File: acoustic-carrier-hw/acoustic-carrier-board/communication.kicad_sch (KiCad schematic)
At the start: 0 parts

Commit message: [acoustic-carrier-board] Added ethernet PHY
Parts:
- added J3: 8P8C_Shielded, Connector_RJ:RJ45_RCH_RC01937, symbol Connector:8P8C_Shielded
- added U1: KSZ9031RNXCA, Package_DFN_QFN:QFN-48-1EP_7x7mm_P0.5mm_EP5.15x5.15mm, symbol Interface_Ethernet:KSZ9031RNXCA
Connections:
- new net GNDA: J3.SH

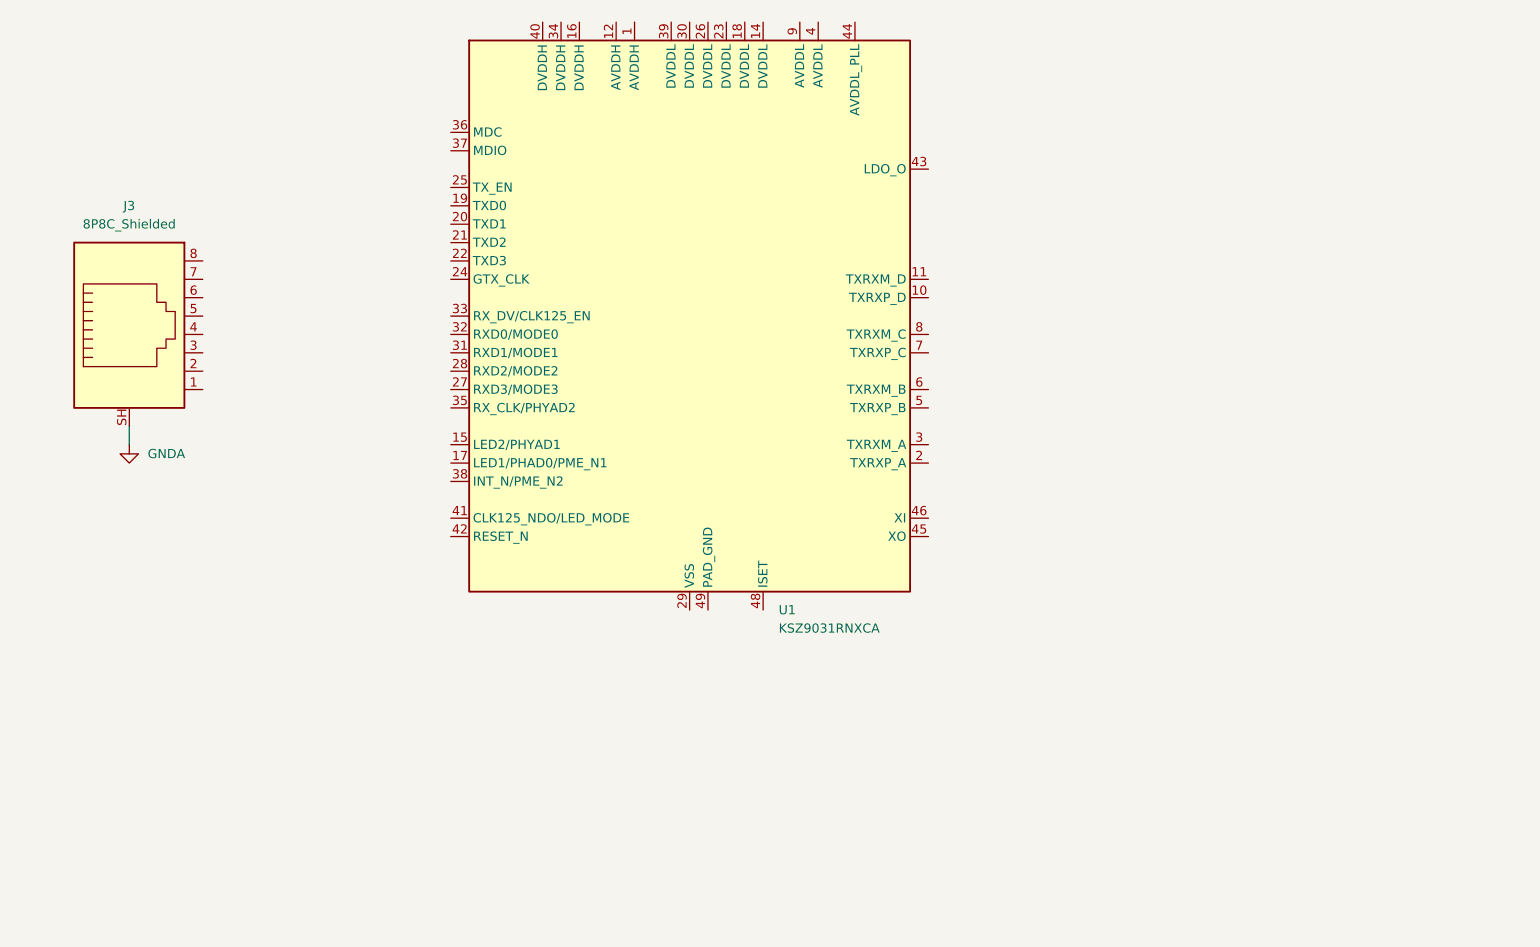
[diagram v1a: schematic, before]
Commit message: [carrier] Added decoupling to ethernet PHY
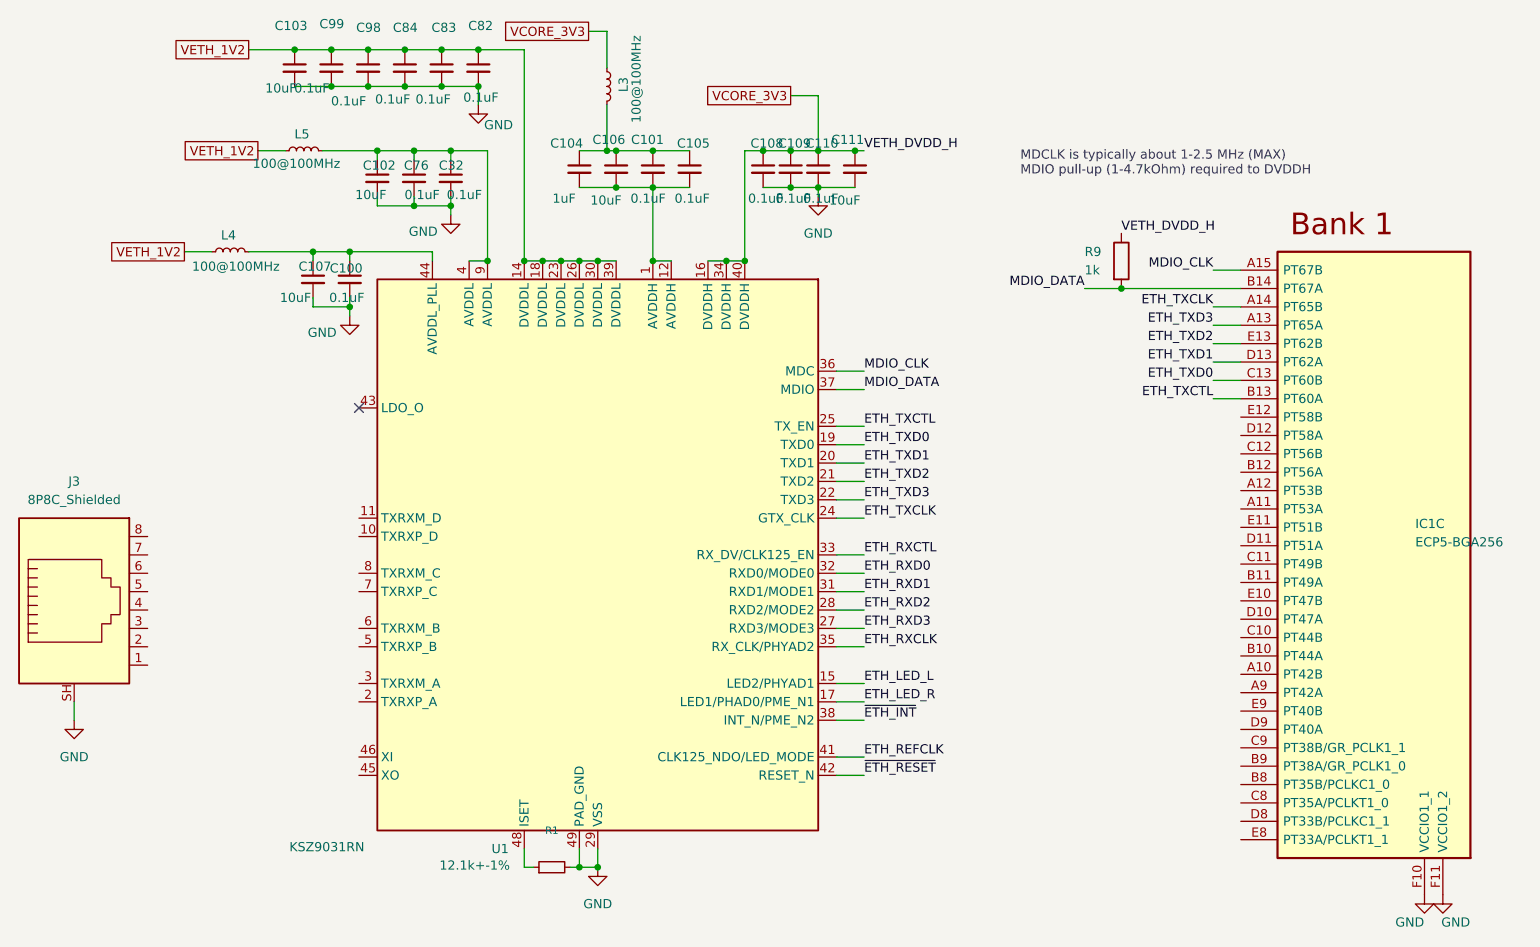
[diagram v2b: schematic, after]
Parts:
- added C100, C101, C105, C108, C109, C110, C32, C76, C82, C83, C84, C98, C99: 0.1uF, Capacitor_SMD:C_0402_1005Metric, symbol Device:C_Small
- added C102, C103, C106, C107, C111: 10uF, Capacitor_SMD:C_0603_1608Metric, symbol Device:C_Small
- added C104: 1uF, Capacitor_SMD:C_0805_2012Metric, symbol Device:C_Small
- added IC1: ECP5-BGA256, BGA256C80P16X16_1400X1400X170, symbol ecp5bga256:ECP5-BGA256
- added L3, L4, L5: 100@100MHz, Inductor_SMD:L_0805_2012Metric, symbol Device:L_Small
- added R1: 12.1k+-1%, Resistor_SMD:R_0603_1608Metric, symbol Device:R_Small
- added R9: 1k, Resistor_SMD:R_0805_2012Metric_Pad1.20x1.40mm_HandSolder, symbol Device:R
- U1: value KSZ9031RNXCA -> KSZ9031RN; LPN (none) -> C461575; MPN (none) -> KSZ9031RNXCC
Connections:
- net GNDA is gone; now on net GND: J3.SH
- net at U1.1 (AVDDH): now also U1.12 (AVDDH), C101.2, C104.2, C105.2, C106.2
- net VETH_1V2: now reaches U1.14 (DVDDL)
- net VETH_1V2: now also U1.18 (DVDDL), U1.23 (DVDDL), U1.26 (DVDDL), U1.30 (DVDDL), U1.39 (DVDDL), C103.1, C82.1, C83.1, C84.1, C98.1, C99.1, L4.2, L5.2
- net ETH_LED_L: now reaches U1.15 (LED2/PHYAD1)
- net VCORE_3V3: now reaches U1.16 (DVDDH)
- net VCORE_3V3: now also U1.34 (DVDDH), U1.40 (DVDDH), C108.1, C109.1, C110.1, C111.1, L3.2, R9.1
- net ETH_LED_R: now reaches U1.17 (LED1/PHAD0/PME_N1)
- net ETH_TXD0: now reaches U1.19 (TXD0)
- net ETH_TXD0: now also IC1.C13 (PT60B)
- net ETH_TXD1: now reaches U1.20 (TXD1)
- net ETH_TXD1: now also IC1.D13 (PT62A)
- net ETH_TXD2: now reaches U1.21 (TXD2)
- net ETH_TXD2: now also IC1.E13 (PT62B)
- net ETH_TXD3: now reaches U1.22 (TXD3)
- net ETH_TXD3: now also IC1.A13 (PT65A)
- net ETH_TXCLK: now reaches U1.24 (GTX_CLK)
- net ETH_TXCLK: now also IC1.A14 (PT65B)
- net ETH_TXCTL: now reaches U1.25 (TX_EN)
- net ETH_TXCTL: now also IC1.B13 (PT60A)
- net ETH_RXD3: now reaches U1.27 (RXD3/MODE3)
- net ETH_RXD2: now reaches U1.28 (RXD2/MODE2)
- net GND: now reaches U1.29 (VSS)
- net GND: now also U1.49 (PAD_GND), C100.2, C102.2, C103.2, C107.2, C108.2, C109.2, C110.2, C111.2, C32.2, C76.2, C82.2, C83.2, C84.2, C98.2, C99.2, IC1.F10 (VCCIO1_1), IC1.F11 (VCCIO1_2), R1.2
- net ETH_RXD1: now reaches U1.31 (RXD1/MODE1)
- net ETH_RXD0: now reaches U1.32 (RXD0/MODE0)
- net ETH_RXCTL: now reaches U1.33 (RX_DV/CLK125_EN)
- net ETH_RXCLK: now reaches U1.35 (RX_CLK/PHYAD2)
- net MDIO_CLK: now reaches U1.36 (MDC)
- net MDIO_CLK: now also IC1.A15 (PT67B)
- net MDIO_DATA: now reaches U1.37 (MDIO)
- net MDIO_DATA: now also IC1.B14 (PT67A), R9.2
- net ~{ETH_INT}: now reaches U1.38 (INT_N/PME_N2)
- net at U1.4 (AVDDL): now also U1.9 (AVDDL), C102.1, C32.1, C76.1, L5.1
- net ETH_REFCLK: now reaches U1.41 (CLK125_NDO/LED_MODE)
- net ~{ETH_RESET}: now reaches U1.42 (RESET_N)
- net at U1.44 (AVDDL_PLL): now also C100.1, C107.1, L4.1
- net at U1.48 (ISET): now also R1.1
- new net: C101.1, C104.1, C105.1, C106.1, L3.1
- no-connect marks 0 -> 1
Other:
- note added: "MDCLK is typically about 1-2.5 MHz (MAX) MDIO pull-up (1-4.7kOhm) required to DVDDH"
- moved on the sheet: J3, U1

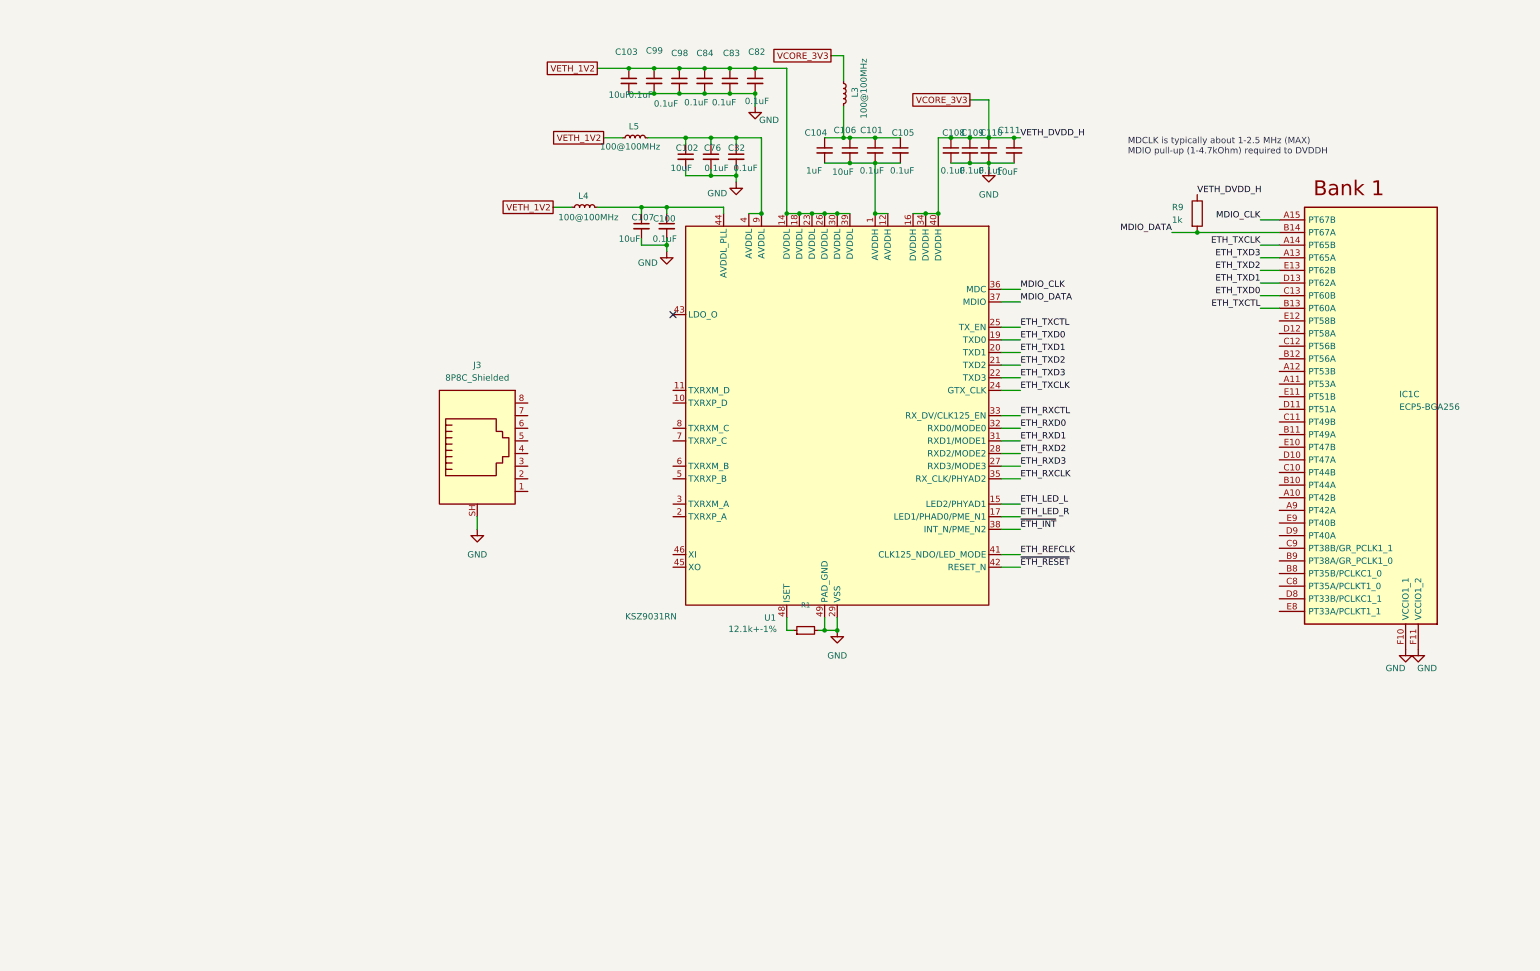
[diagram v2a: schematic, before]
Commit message: [carrier] Finished ethernet
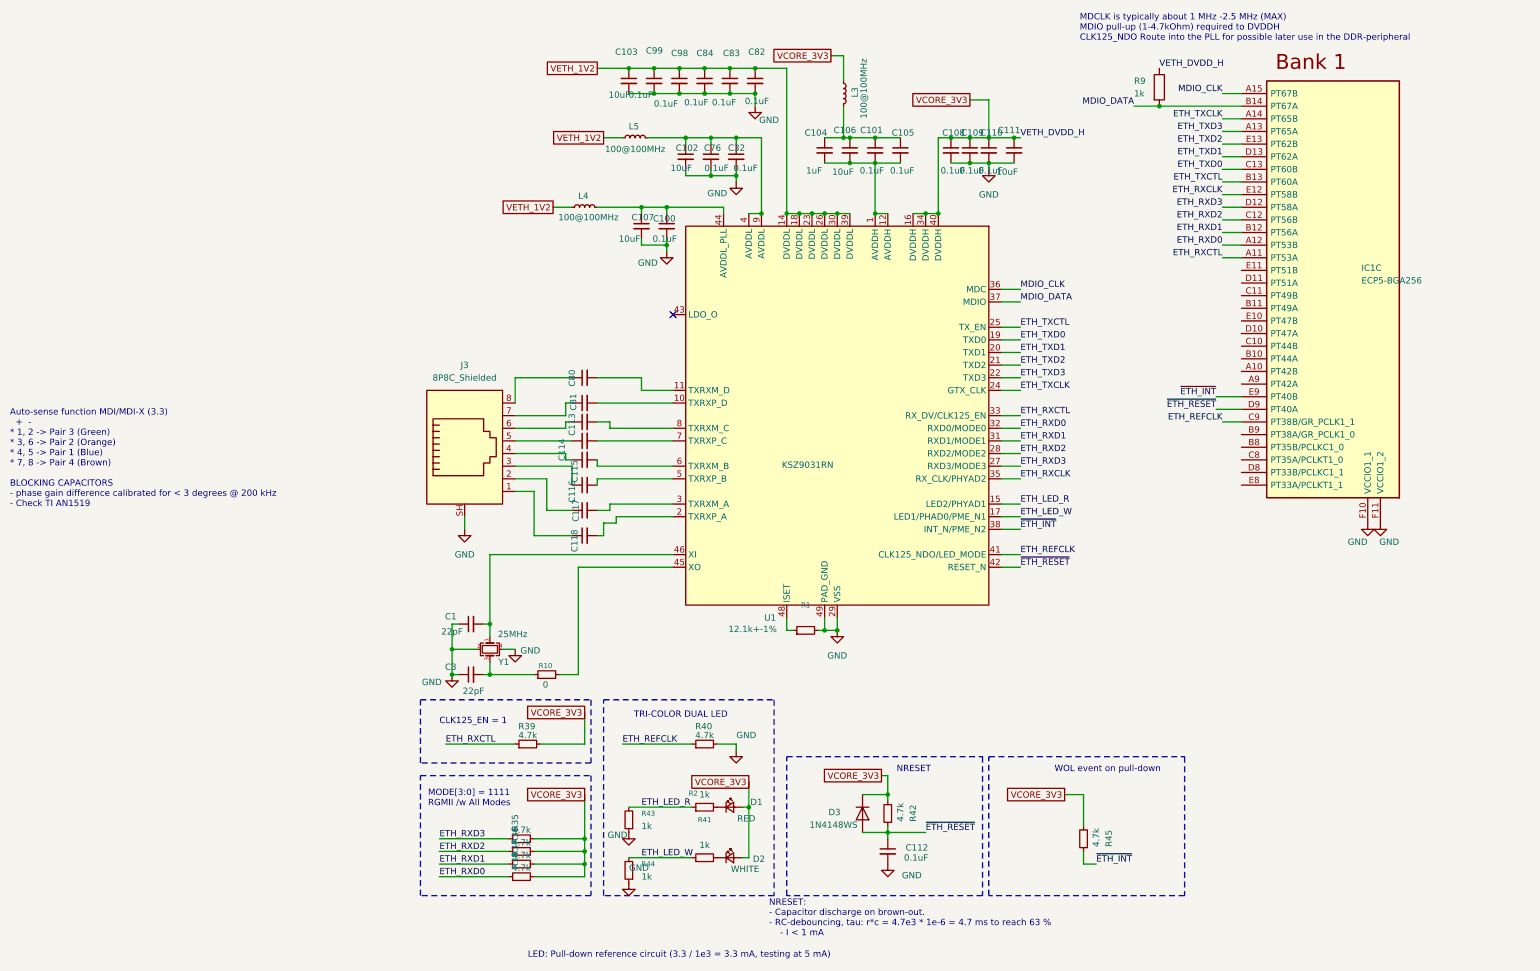
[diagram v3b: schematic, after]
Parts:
- added C1, C3: 22pF, Capacitor_SMD:C_0402_1005Metric, symbol Device:C_Small
- added C112: 0.1uF, Capacitor_SMD:C_0402_1005Metric, symbol Device:C_Small
- added C113, C114, C115, C116, C117, C118, C80, C81: 100 nF +-5%, Capacitor_SMD:C_0603_1608Metric_Pad1.08x0.95mm_HandSolder, symbol Device:C_Small
- added D1: RED, Diode_SMD:D_0603_1608Metric, symbol Device:LED_Small
- added D2: WHITE, Diode_SMD:D_0603_1608Metric, symbol Device:LED_Small
- added D3: 1N4148WS, Diode_SMD:D_SOD-323, symbol Diode:1N4148WS
- added R10: 0, Resistor_SMD:R_0402_1005Metric_Pad0.72x0.64mm_HandSolder, symbol Device:R_Small
- added R2, R41, R43, R44: 1k, Resistor_SMD:R_0402_1005Metric, symbol Device:R_Small
- added R35, R36, R37, R38, R39, R40, R42, R45: 4.7k, Resistor_SMD:R_0402_1005Metric, symbol Device:R_Small
- added Y1: 25MHz, Crystal:Crystal_SMD_3225-4Pin_3.2x2.5mm, symbol Device:Crystal_GND24_Small
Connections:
- net ETH_LED_L is gone; now on net ETH_LED_R: U1.15 (LED2/PHYAD1)
- net ETH_LED_R: now also R2.1, R43.2; no longer U1.17 (LED1/PHAD0/PME_N1)
- net ETH_REFCLK: now also IC1.C9 (PT38B/GR_PCLK1_1), R40.1
- net ETH_RXCLK: now also IC1.E12 (PT58B)
- net ETH_RXCTL: now also IC1.A11 (PT53A), R39.1
- net ETH_RXD0: now also IC1.A12 (PT53B), R38.1
- net ETH_RXD1: now also IC1.B12 (PT56A), R37.1
- net ETH_RXD2: now also IC1.C12 (PT56B), R36.1
- net ETH_RXD3: now also IC1.D12 (PT58A), R35.1
- net GND: now also C1.1, C112.2, C3.1, R40.2, R43.1, R44.1, Y1.2, Y1.4
- net VCORE_3V3: now also D1.2 (A), D2.2 (A), D3.1 (K), R35.2, R36.2, R37.2, R38.2, R39.2, R42.2, R45.2
- net ~{ETH_INT}: now also IC1.E9 (PT40B), R45.1
- net ~{ETH_RESET}: now also IC1.D9 (PT40A), C112.1, D3.2 (A), R42.1
- net at J3.1: now also C118.1
- net at J3.2: now also C117.1
- net at J3.3: now also C116.1
- net at J3.4: now also C115.1
- net at J3.5: now also C114.1
- net at J3.6: now also C113.1
- net at J3.7: now also C81.1
- net at J3.8: now also C80.1
- net at U1.10 (TXRXP_D): now also C81.2
- net at U1.11 (TXRXM_D): now also C80.2
- net at U1.2 (TXRXP_A): now also C118.2
- net at U1.3 (TXRXM_A): now also C117.2
- net at U1.45 (XO): now also R10.2
- net at U1.46 (XI): now also C1.2, Y1.1
- net at U1.5 (TXRXP_B): now also C116.2
- net at U1.6 (TXRXM_B): now also C115.2
- net at U1.7 (TXRXP_C): now also C114.2
- net at U1.8 (TXRXM_C): now also C113.2
- new net: C3.2, R10.1, Y1.3
- new net: D1.1 (K), R2.2
- new net: D2.1 (K), R41.2
- new net ETH_LED_W: R41.1, R44.2, U1.17 (LED1/PHAD0/PME_N1)
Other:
- note added: "Auto-sense function MDI/MDI-X (3.3) + - * 1, 2 -> Pair 3 (Green) * 3, 6 -> Pair 2 (Orange) * 4, 5 -> Pair 1 (Blue) * 7, 8 -> Pair 4 (Brown) BLOCKING CAPACITORS - phase gain difference calibrated for < 3 degrees @ 200 kHz - Check TI AN1519"
- note added: "CLK125_EN = 1"
- note added: "LED: Pull-down reference circuit (3.3 / 1e3 = 3.3 mA, testing at 5 mA)"
- note added: "MDCLK is typically about 1 MHz -2.5 MHz (MAX) MDIO pull-up (1-4.7kOhm) required to DVDDH CLK125_NDO Route into the PLL for possible later use in the DDR-peripheral"
- note added: "MODE[3:0] = 1111 RGMII /w All Modes"
- note added: "NRESET"
- note added: "NRESET: - Capacitor discharge on brown-out. - RC-debouncing, tau: r*c = 4.7e3 * 1e-6 = 4.7 ms to reach 63 % - I < 1 mA"
- note added: "TRI-COLOR DUAL LED"
- note added: "WOL event on pull-down"
- note removed: "MDCLK is typically about 1-2.5 MHz (MAX) MDIO pull-up (1-4.7kOhm) required to DVDDH"
- moved on the sheet: IC1C, J3, R9

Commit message: [carrier] Added usb power + communication circuitry (next) Connect ADC pins to bank 0, select PWM pins, check connectors for power board
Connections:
- net USB_SENSE: now reaches IC1.B11 (PT49A)
- net USB_RENUMn: now reaches IC1.C11 (PT49B)
- net FPGA_USB_RX: now reaches IC1.D11 (PT51A)
- net FPGA_USB_TX: now reaches IC1.E11 (PT51B)
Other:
- added sheet usb (usb.kicad_sch)
- note added: "Auto-sense function MDI/MDI-X (3.3) + - * 1, 2 -> Pair 3 (Green) * 3, 6 -> Pair 2 (Orange) * 4, 5 -> Pair 1 (Blue) * 7, 8 -> Pair 4 (Brown) BLOCKING CAPACITORS - phase gain difference calibrated for < 3 degrees @ 200 kHz - Check TI AN1519 However: the self-resonance of these ethernet magnetics is probably way below 1 GHz. - For now keep the 100 nF S.R.F -> think about using magnetics later-on"
- note removed: "Auto-sense function MDI/MDI-X (3.3) + - * 1, 2 -> Pair 3 (Green) * 3, 6 -> Pair 2 (Orange) * 4, 5 -> Pair 1 (Blue) * 7, 8 -> Pair 4 (Brown) BLOCKING CAPACITORS - phase gain difference calibrated for < 3 degrees @ 200 kHz - Check TI AN1519"
- moved on the sheet: IC1C, R9
